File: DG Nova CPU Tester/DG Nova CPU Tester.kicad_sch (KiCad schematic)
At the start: 114 parts, among them J1 Slot_02x50_Odd_Even, J10 Programmed I/O, J11 CPU Option Inputs, J12 Data Channel, J13 Program Interrupt, J14 System Control, J17 CPU Option Outputs, J18 MEM Control Outputs, J19 Logic 8 CH, J20 Logic 8 CH, J21 Arduino Anolog Pins, J22 Arduino Digital Pins, J23 Arduino Digital Pins, J4 ATX-24, J6 MBO, J7 MEM, J8 Data Channel, J9 Front Panel Controls, SW1 SW_Push, U1 74HC14, U2 Pico

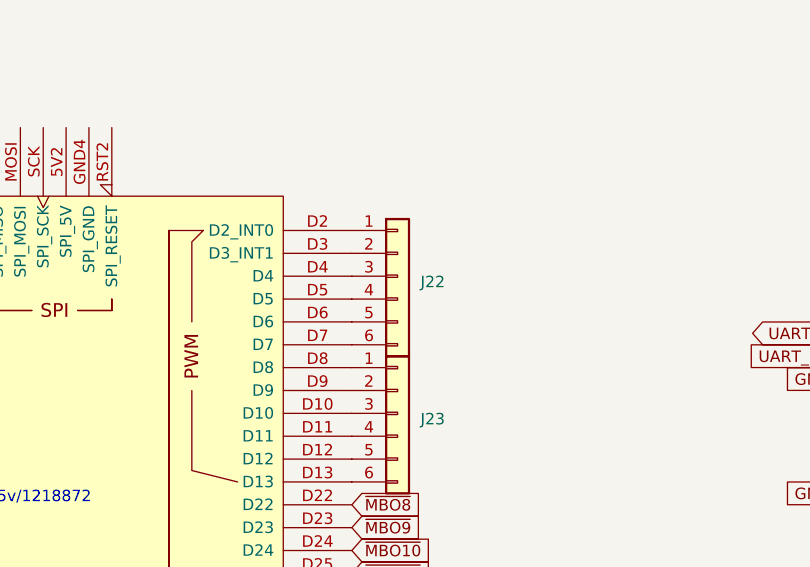
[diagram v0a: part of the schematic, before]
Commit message: All the Control Panel Lights, but still not the Front Panel Connectors
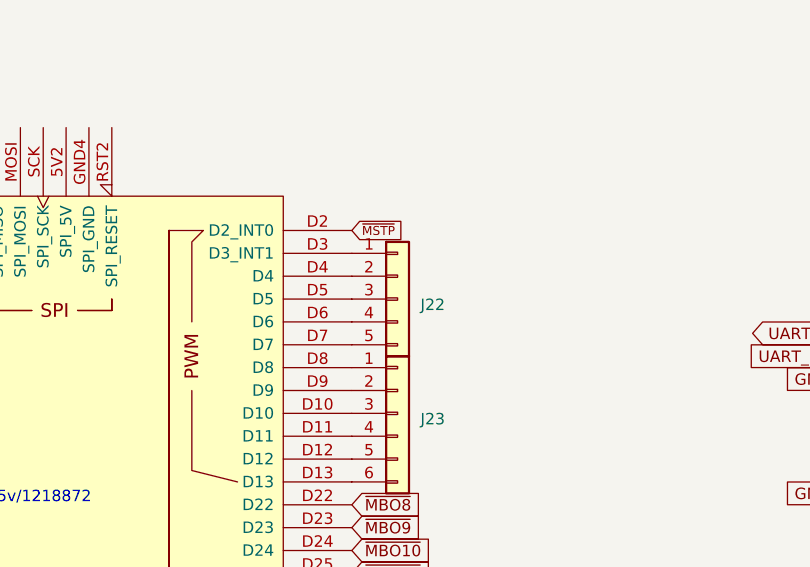
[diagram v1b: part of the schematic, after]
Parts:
- J22: footprint Connector_PinHeader_2.54mm:PinHeader_1x06_P2.54mm_Vertical -> Connector_PinHeader_2.54mm:PinHeader_1x05_P2.54mm_Vertical; symbol Connector_Generic:Conn_01x06 -> Connector_Generic:Conn_01x05
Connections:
- net ~{MSTP}: now also XA1.D2 (D2_INT0)
- net at J22.1 (Pin_1): now also XA1.D3 (D3_INT1); no longer XA1.D2 (D2_INT0)
- net at J22.2 (Pin_2): now also XA1.D4; no longer XA1.D3 (D3_INT1)
- net at J22.3 (Pin_3): now also XA1.D5; no longer XA1.D4
- net at J22.4 (Pin_4): now also XA1.D6; no longer XA1.D5
- net at J22.5 (Pin_5): now also XA1.D7; no longer XA1.D6
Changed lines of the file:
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@@
     )
   )
+  (global_label "~{MSTP}" (shape input) (at 213.36 167.005 0) (fields_autoplaced)
+    (effects (font (size 0.9906 0.9906)) (justify left))
+    (property "Intersheetrefs" "${INTERSHEET_REFS}" (at 218.937 167.005 0)
+      (effects (font (size 1.27 1.27)) (justify left) hide)
+    )
+  )
   (global_label "~{SHIFT1}" (shape input) (at 329.565 323.85 270) (fields_autoplaced)
     (effects (font (size 1.27 1.27)) (justify right))
@@
     )
   )
-  (symbol (lib_id "Connector_Generic:Conn_01x06") (at 218.44 172.085 0) (unit 1)
+  (symbol (lib_id "Connector_Generic:Conn_01x05") (at 218.44 174.625 0) (unit 1)
     (in_bom yes) (on_board yes) (dnp no) (fields_autoplaced)
-    (property "Reference" "J22" (at 220.98 172.72 0)
+    (property "Reference" "J22" (at 220.98 175.26 0)
       (effects (font (size 1.27 1.27)) (justify left))
     )
-    (property "Value" "Arduino Digital Pins" (at 220.98 175.26 0)
+    (property "Value" "Arduino Digital Pins" (at 220.98 177.8 0)
       (effects (font (size 1.27 1.27)) (justify left) hide)
     )
-    (property "Footprint" "Connector_PinHeader_2.54mm:PinHeader_1x06_P2.54mm_Vertical" (at 218.44 172.085 0)
+    (property "Footprint" "Connector_PinHeader_2.54mm:PinHeader_1x05_P2.54mm_Vertical" (at 218.44 174.625 0)
       (effects (font (size 1.27 1.27)) hide)
     )
-    (property "Datasheet" "~" (at 218.44 172.085 0)
+    (property "Datasheet" "~" (at 218.44 174.625 0)
       (effects (font (size 1.27 1.27)) hide)
     )
@@
     (pin "4")
     (pin "5")
-    (pin "6")
     (instances
       (project "DG Nova CPU Tester"

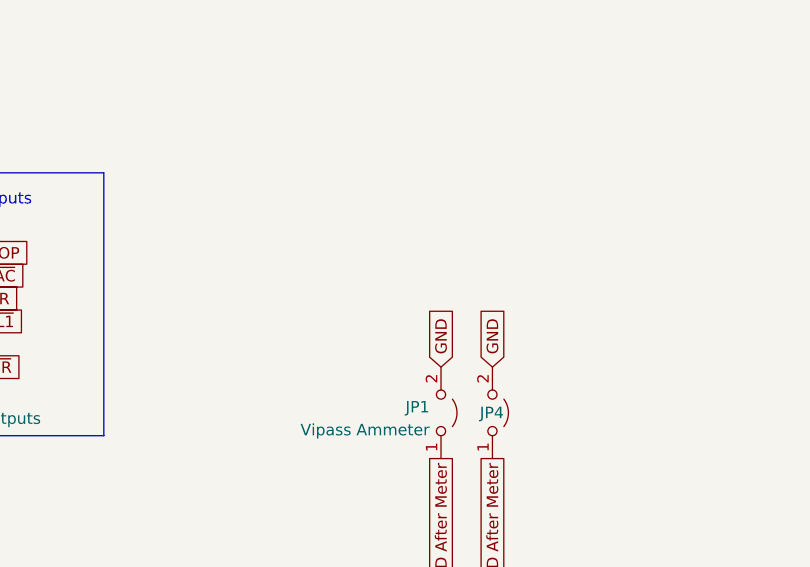
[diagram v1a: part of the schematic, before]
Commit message: Done right BEFORE Ground & 5v Fill
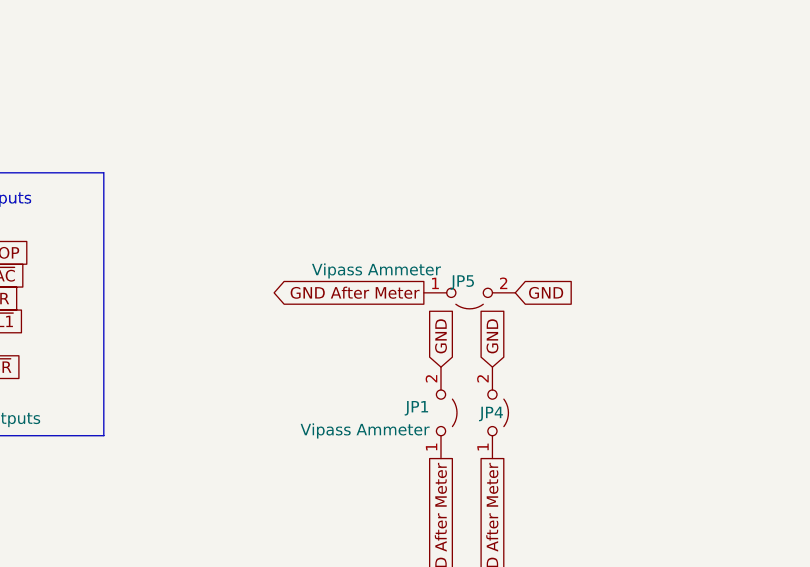
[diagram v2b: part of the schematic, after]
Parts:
- added JP5: Vipass Ammeter, Connector_PinHeader_2.54mm:PinHeader_1x02_P2.54mm_Vertical, symbol Jumper:Jumper_2_Open
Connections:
- net GND: now also JP5.2 (B)
- net GND After Meter: now also JP5.1 (A)
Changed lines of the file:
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@@
     )
   )
+  (global_label "GND After Meter" (shape output) (at 343.535 29.21 180) (fields_autoplaced)
+    (effects (font (size 1.27 1.27)) (justify right))
+    (property "Intersheetrefs" "${INTERSHEET_REFS}" (at 325.843 29.21 0)
+      (effects (font (size 1.27 1.27)) (justify right) hide)
+    )
+  )
   (global_label "~{WAS JSR}" (shape input) (at 288.925 37.465 0) (fields_autoplaced)
     (effects (font (size 1.27 1.27)) (justify left))
@@
     )
   )
+  (global_label "GND" (shape input) (at 353.695 29.21 0) (fields_autoplaced)
+    (effects (font (size 1.27 1.27)) (justify left))
+    (property "Intersheetrefs" "${INTERSHEET_REFS}" (at 359.8965 29.21 0)
+      (effects (font (size 1.27 1.27)) (justify left) hide)
+    )
+  )
   (global_label "~{SELB}" (shape input) (at 193.04 62.23 0) (fields_autoplaced)
     (effects (font (size 1.27 1.27)) (justify left))
@@
         )
       )
+    )
+  )
+  (symbol (lib_id "Jumper:Jumper_2_Open") (at 348.615 29.21 0) (mirror x) (unit 1)
+    (in_bom yes) (on_board yes) (dnp no)
+    (property "Reference" "JP5" (at 349.25 27.94 0)
+      (effects (font (size 1.27 1.27)) (justify right))
+    )
+    (property "Value" "Vipass Ammeter" (at 345.44 26.67 0)
+      (effects (font (size 1.27 1.27)) (justify right))
+    )
+    (property "Footprint" "Connector_PinHeader_2.54mm:PinHeader_1x02_P2.54mm_Vertical" (at 348.615 29.21 0)
+      (effects (font (size 1.27 1.27)) hide)
+    )
+    (property "Datasheet" "~" (at 348.615 29.21 0)
+      (effects (font (size 1.27 1.27)) hide)
+    )
+    (pin "1")
+    (pin "2")
+    (instances
+      (project "DG Nova CPU Tester"
+        (path "/c1f710ce-b3f9-4828-9325-9c2326e8d74c"
+          (reference "JP5") (unit 1)
+        )
+      )

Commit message: Did I get lost?
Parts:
- added 3v3: 3v3, Connector_PinHeader_2.54mm:PinHeader_1x04_P2.54mm_Vertical, symbol Connector_Generic:Conn_01x04
- added SW2: Power Swtich, Button_Switch_THT:SW_E-Switch_EG1271_SPDT, symbol Switch:SW_Push_DPDT
- added Teensy 4.1: Teensy4.1, Forgotten Machines:Teensy41, symbol ForgottenMachines:Teensy4.1
- BAR1: footprint Display:HDSP-4832 -> Forgotten Machines:LED Bar 10
- C1: value CAP_Disc_Common_-_Entrex_Trapezoid -> ~{PL} Backplane Cap
- C2: value CAP_Disc_Common_-_Entrex_Trapezoid -> ~{CON RQ} Backplane Cap
- J17: footprint Connector_PinHeader_2.54mm:PinHeader_1x05_P2.54mm_Vertical -> Connector_PinHeader_2.54mm:PinHeader_1x06_P2.54mm_Vertical
- J4: value ATX-24 -> ATX Power Port
- SW1: value SW_Push -> Arduino Mega Reset
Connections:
- net +3v3: now also 3v3.1 (Pin_1), 3v3.2 (Pin_2), 3v3.3 (Pin_3), 3v3.4 (Pin_4)
- net +5V: now also Teensy 4.1.48 (VIN)
- net +5V OK: now also J23.6 (Pin_6), XA1.D13
- net GND: now also SW2.1 (A), SW2.2 (B), SW2.4 (A), SW2.5 (B), Teensy 4.1.1 (GND), Teensy 4.1.34 (GND), Teensy 4.1.47 (GND), Teensy 4.1.52 (GND), Teensy 4.1.58 (GND), Teensy 4.1.59 (GND), Teensy 4.1.64 (GND)
- net Power SW: now also SW2.3 (C), SW2.6 (C)
- net ~{POWER FAIL}: now also XA1.D53 (D53_SS)
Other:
- note added: "Power-Up Signal Manager"
- note added: "See the Entrex 480 Front Panel schematic"
- note removed: "Start-Up Power Manager"
- moved on the sheet: JP1, JP4, JP5, MES1, TP1

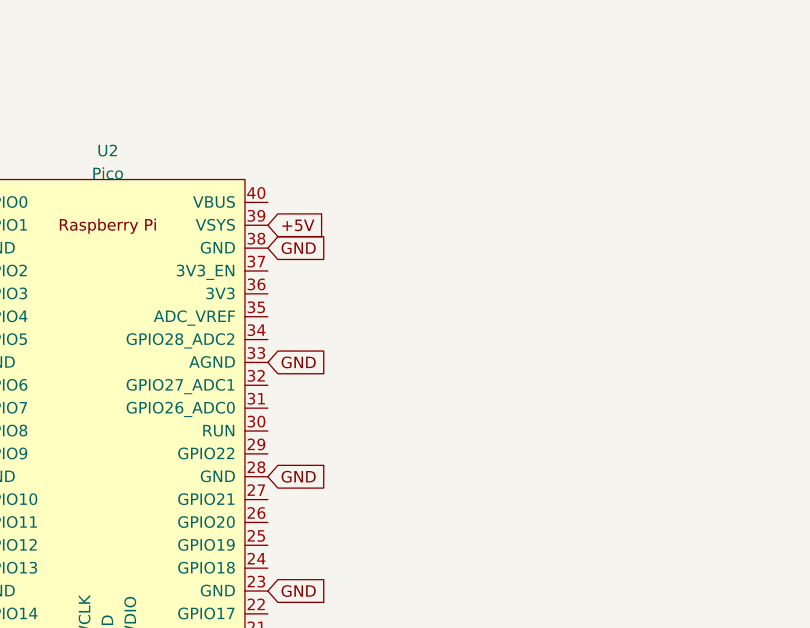
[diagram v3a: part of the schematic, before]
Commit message: Add Reset Button & Shottky Diode to Pico
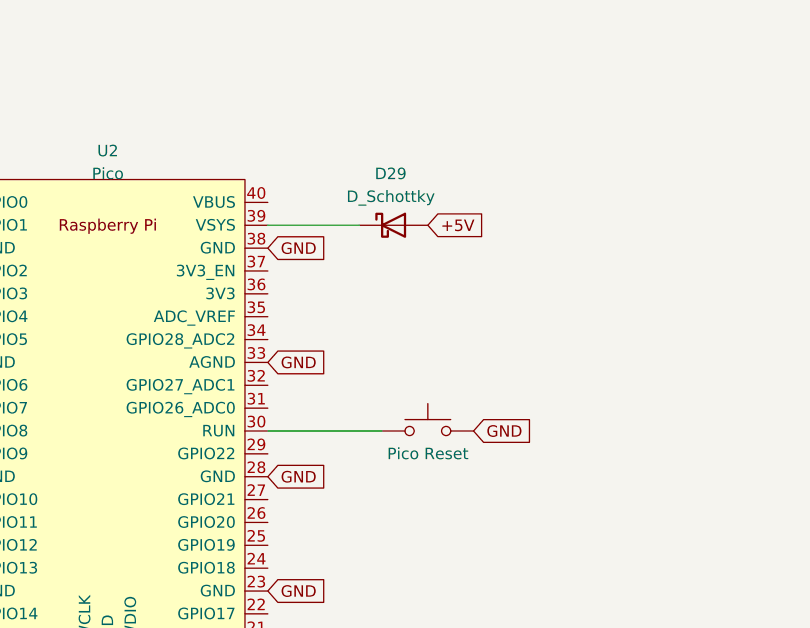
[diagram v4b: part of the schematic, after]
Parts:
- added D29: D_Schottky, Diode_THT:D_DO-35_SOD27_P10.16mm_Horizontal, symbol Device:D_Schottky
- added SW1: Pico Reset, Button_Switch_THT:SW_PUSH_6mm, symbol Switch:SW_Push
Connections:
- net +5V: now also D29.2 (A); no longer U2.39 (VSYS)
- net GND: now also SW1.1
- net at U2.30 (RUN): now also SW1.2
- new net: D29.1 (K), U2.39 (VSYS)
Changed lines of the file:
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@@
     (stroke (width 0) (type default))
   )
+  (wire (pts (xy 303.53 203.835) (xy 316.23 203.835))
+    (stroke (width 0) (type default))
+  )
   (wire (pts (xy 200.025 -21.59) (xy 205.105 -21.59))
     (stroke (width 0) (type default))
@@
     (stroke (width 0) (type default))
   )
+  (wire (pts (xy 303.53 180.975) (xy 313.69 180.975))
+    (stroke (width 0) (type default))
+  )
   (wire (pts (xy 161.29 469.9) (xy 161.29 478.79))
     (stroke (width 0) (type default))
@@
     )
   )
-  (global_label "+5V" (shape input) (at 303.53 180.975 0) (fields_autoplaced)
+  (global_label "+5V" (shape input) (at 321.31 180.975 0) (fields_autoplaced)
     (effects (font (size 1.27 1.27)) (justify left))
-    (property "Intersheetrefs" "${INTERSHEET_REFS}" (at 309.6521 180.975 0)
+    (property "Intersheetrefs" "${INTERSHEET_REFS}" (at 327.4321 180.975 0)
       (effects (font (size 1.27 1.27)) (justify left) hide)
     )
@@
     )
   )
+  (global_label "GND" (shape input) (at 326.39 203.835 0) (fields_autoplaced)
+    (effects (font (size 1.27 1.27)) (justify left))
+    (property "Intersheetrefs" "${INTERSHEET_REFS}" (at 332.5121 203.835 0)
+      (effects (font (size 1.27 1.27)) (justify left) hide)
+    )
+  )
   (global_label "~{MBO7}" (shape input) (at 42.545 177.165 180) (fields_autoplaced)
     (effects (font (size 1.27 1.27)) (justify right))
@@
     )
   )
+  (symbol (lib_id "Device:D_Schottky") (at 317.5 180.975 0) (unit 1)
+    (in_bom yes) (on_board yes) (dnp no) (fields_autoplaced)
+    (property "Reference" "D29" (at 317.1825 175.26 0)
+      (effects (font (size 1.27 1.27)))
+    )
+    (property "Value" "D_Schottky" (at 317.1825 177.8 0)
+      (effects (font (size 1.27 1.27)))
+    )
+    (property "Footprint" "Diode_THT:D_DO-35_SOD27_P10.16mm_Horizontal" (at 317.5 180.975 0)
+      (effects (font (size 1.27 1.27)) hide)
+    )
+    (property "Datasheet" "~" (at 317.5 180.975 0)
+      (effects (font (size 1.27 1.27)) hide)
+    )
+    (pin "2")
+    (pin "1")
+    (instances
+      (project "DG Nova CPU Tester"
+        (path "/c1f710ce-b3f9-4828-9325-9c2326e8d74c"
+          (reference "D29") (unit 1)
+        )
+      )
+    )
+  )
   (symbol (lib_id "ForgottenMachines:ATX-24") (at 386.715 76.835 0) (unit 1)
     (in_bom yes) (on_board yes) (dnp no) (fields_autoplaced)
@@
         )
       )
+    )
+  )
+  (symbol (lib_id "Switch:SW_Push") (at 321.31 203.835 0) (mirror y) (unit 1)
+    (in_bom yes) (on_board yes) (dnp no)
+    (property "Reference" "SW1" (at 321.31 198.755 0)
+      (effects (font (size 1.27 1.27)) hide)
+    )
+    (property "Value" "Pico Reset" (at 321.31 206.375 0)
+      (effects (font (size 1.27 1.27)))
+    )
+    (property "Footprint" "Button_Switch_THT:SW_PUSH_6mm" (at 321.31 198.755 0)
+      (effects (font (size 1.27 1.27)) hide)
+    )
+    (property "Datasheet" "~" (at 321.31 198.755 0)
+      (effects (font (size 1.27 1.27)) hide)
+    )
+    (pin "1")
+    (pin "2")
+    (instances
+      (project "DG_Nova_Front_Panel_Tester"
+        (path "/a9be2a60-481e-41e0-b07e-ab1c9808fd0d"
+          (reference "SW1") (unit 1)
+        )
+      )
+      (project "DG Nova CPU Tester"
+        (path "/c1f710ce-b3f9-4828-9325-9c2326e8d74c"
+          (reference "SW3") (unit 1)
+        )
+      )

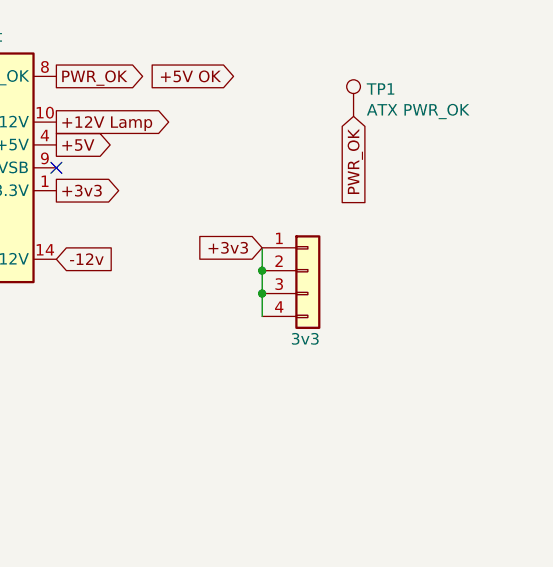
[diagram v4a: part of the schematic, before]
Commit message: Some DRC Cleanup, add 3v3 to back board
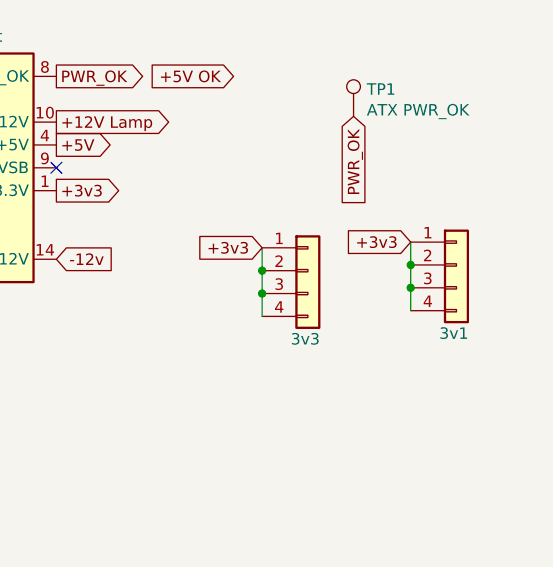
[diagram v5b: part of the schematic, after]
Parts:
- added 3v1: 3v3, Connector_PinHeader_2.54mm:PinHeader_1x04_P2.54mm_Vertical, symbol Connector_Generic:Conn_01x04
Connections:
- net +3v3: now also 3v1.1 (Pin_1), 3v1.2 (Pin_2), 3v1.3 (Pin_3), 3v1.4 (Pin_4)
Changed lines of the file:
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@@
   (junction (at 422.275 90.805) (diameter 0) (color 0 0 0 0)
   )
+  (junction (at 438.785 87.63) (diameter 0) (color 0 0 0 0)
+  )
   (junction (at 236.22 113.03) (diameter 0) (color 0 0 0 0)
   )
@@
   (junction (at 260.985 491.49) (diameter 0) (color 0 0 0 0)
   )
+  (junction (at 438.785 90.17) (diameter 0) (color 0 0 0 0)
+  )
   (junction (at 161.29 491.49) (diameter 0) (color 0 0 0 0)
   )
@@
     (stroke (width 0) (type default))
   )
+  (wire (pts (xy 438.785 87.63) (xy 438.785 90.17))
+    (stroke (width 0) (type default))
+  )
   (wire (pts (xy 123.19 230.505) (xy 147.32 230.505))
     (stroke (width 0) (type default))
@@
     (stroke (width 0) (type default))
   )
+  (wire (pts (xy 438.785 85.09) (xy 438.785 87.63))
+    (stroke (width 0) (type default))
+  )
   (wire (pts (xy 219.71 94.615) (xy 222.885 94.615))
     (stroke (width 0) (type default))
@@
     (stroke (width 0) (type default))
   )
+  (wire (pts (xy 438.785 90.17) (xy 438.785 92.71))
+    (stroke (width 0) (type default))
+  )
   (wire (pts (xy 260.985 469.9) (xy 260.985 478.79))
     (stroke (width 0) (type default))
@@
     )
   )
+  (global_label "+3v3" (shape input) (at 438.785 85.09 180) (fields_autoplaced)
+    (effects (font (size 1.27 1.27)) (justify right))
+    (property "Intersheetrefs" "${INTERSHEET_REFS}" (at 431.495 85.09 0)
+      (effects (font (size 1.27 1.27)) (justify right) hide)
+    )
+  )
   (global_label "~{MBO15}" (shape input) (at 64.135 2.54 180) (fields_autoplaced)
     (effects (font (size 1.27 1.27)) (justify right))
@@
         )
       )
+    )
+  )
+  (symbol (lib_id "Connector_Generic:Conn_01x04") (at 443.865 87.63 0) (unit 1)
+    (in_bom yes) (on_board yes) (dnp no)
+    (property "Reference" "3v1" (at 441.96 95.25 0)
+      (effects (font (size 1.27 1.27)) (justify left))
+    )
+    (property "Value" "3v3" (at 446.405 90.805 0)
+      (effects (font (size 1.27 1.27)) (justify left) hide)
+    )
+    (property "Footprint" "Connector_PinHeader_2.54mm:PinHeader_1x04_P2.54mm_Vertical" (at 443.865 87.63 0)
+      (effects (font (size 1.27 1.27)) hide)
+    )
+    (property "Datasheet" "~" (at 443.865 87.63 0)
+      (effects (font (size 1.27 1.27)) hide)
+    )
+    (pin "1")
+    (pin "2")
+    (pin "3")
+    (pin "4")
+    (instances
+      (project "DG Nova CPU Tester"
+        (path "/c1f710ce-b3f9-4828-9325-9c2326e8d74c"
+          (reference "3v1") (unit 1)
+        )
+      )
